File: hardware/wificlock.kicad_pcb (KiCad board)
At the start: 4 copper layers, 71.8 x 30.5 mm, 41 parts, among them J1 USB_C_Receptacle_USB2.0, Q1 AO3402, Q2 AO3402, Q3 AO3402, Q4 AO3402, SW1 SW_SPST, SW2 SW_SPST, SW3 SW_SPST, U1 CH340C/G, U2 ESP-12F, U3 ME6211C33M5G, U4 HT16K33-20SOP, U5 KW4-56NCLB-P, Y1 12MHz

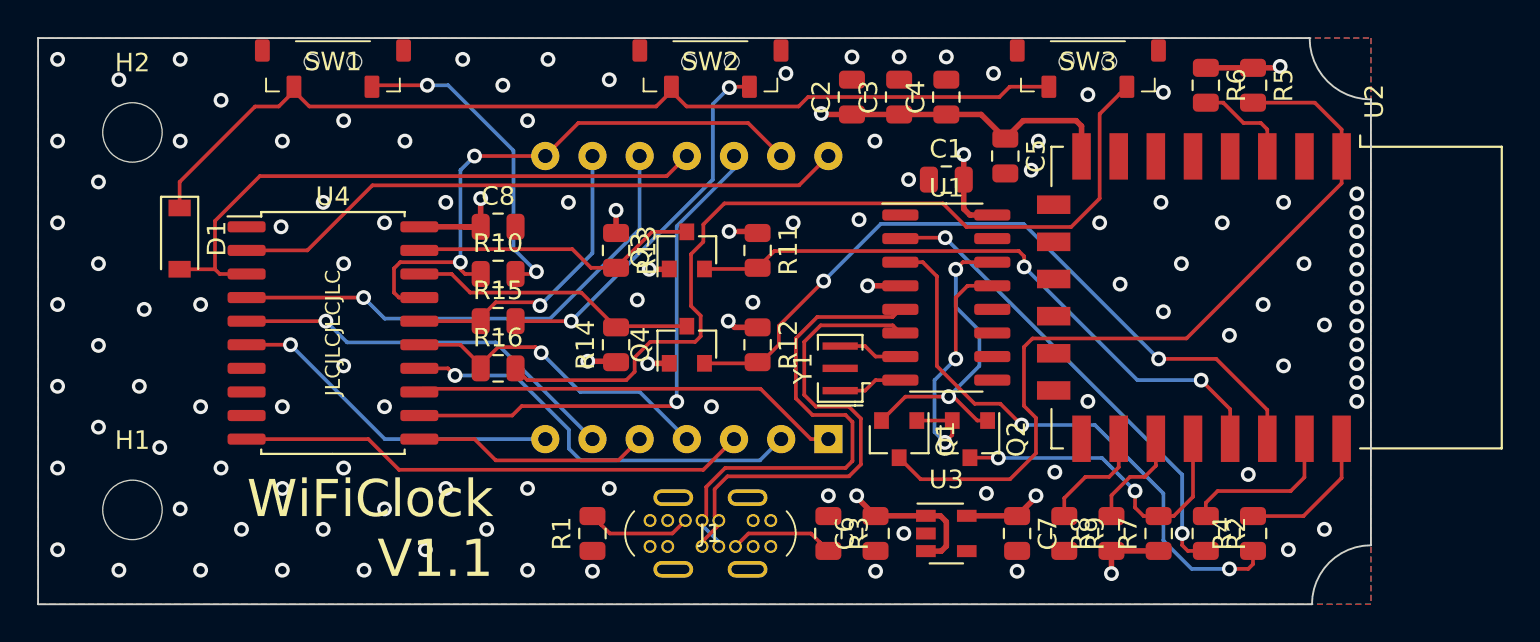
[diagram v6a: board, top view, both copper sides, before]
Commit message: update files after KiCad update
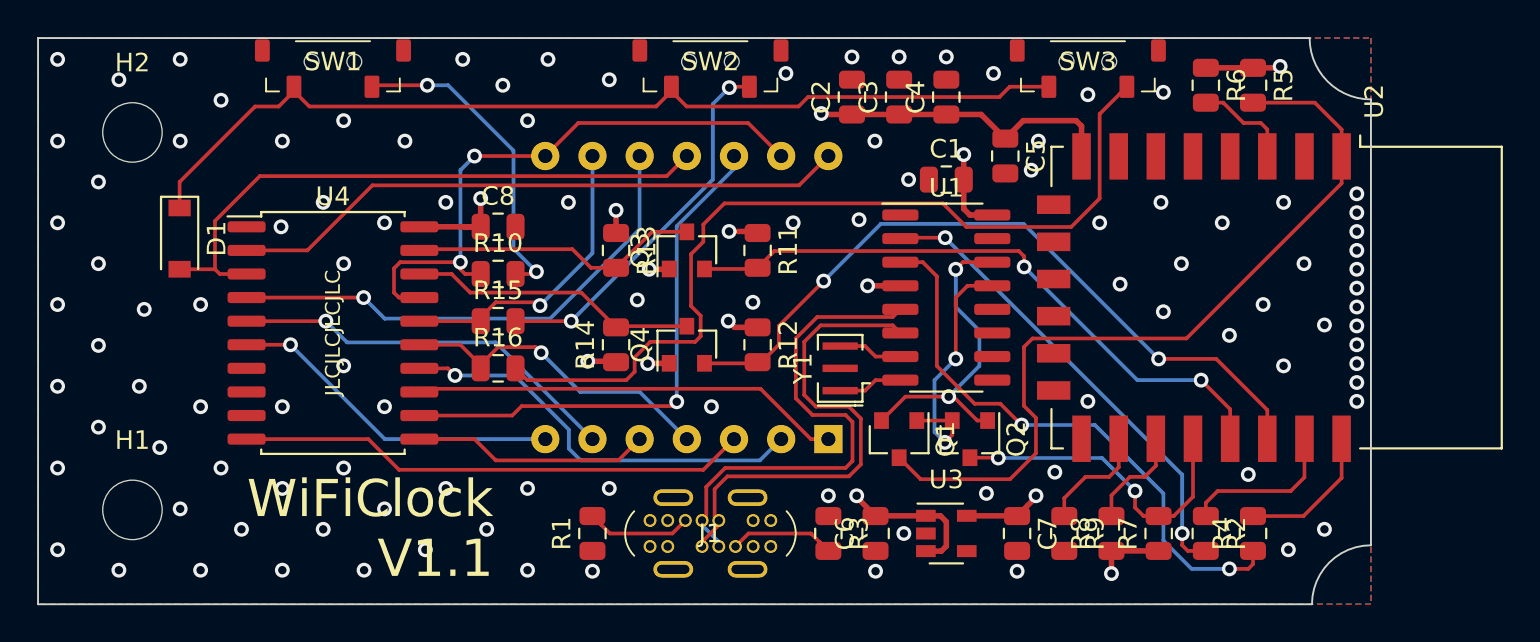
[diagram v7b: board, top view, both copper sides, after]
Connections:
- net ~DTR renamed ~{DTR}
- net ~RST renamed ~{RST}
- net ~RTS renamed ~{RTS}
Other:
- net class Default removed
- net class Power removed
- net class Shield removed
